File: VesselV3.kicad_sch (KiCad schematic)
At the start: 376 parts, among them J1 JTAG/SWD 10pins Headers, Y1 25MHz

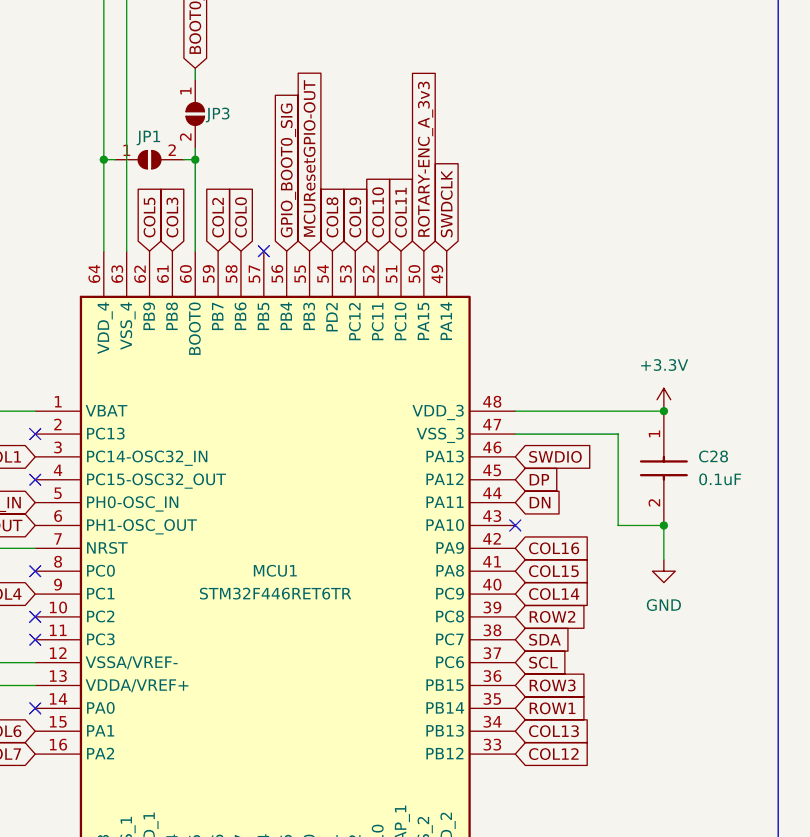
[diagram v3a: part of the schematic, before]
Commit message: FMPI²c to I²c Swap and routing fix
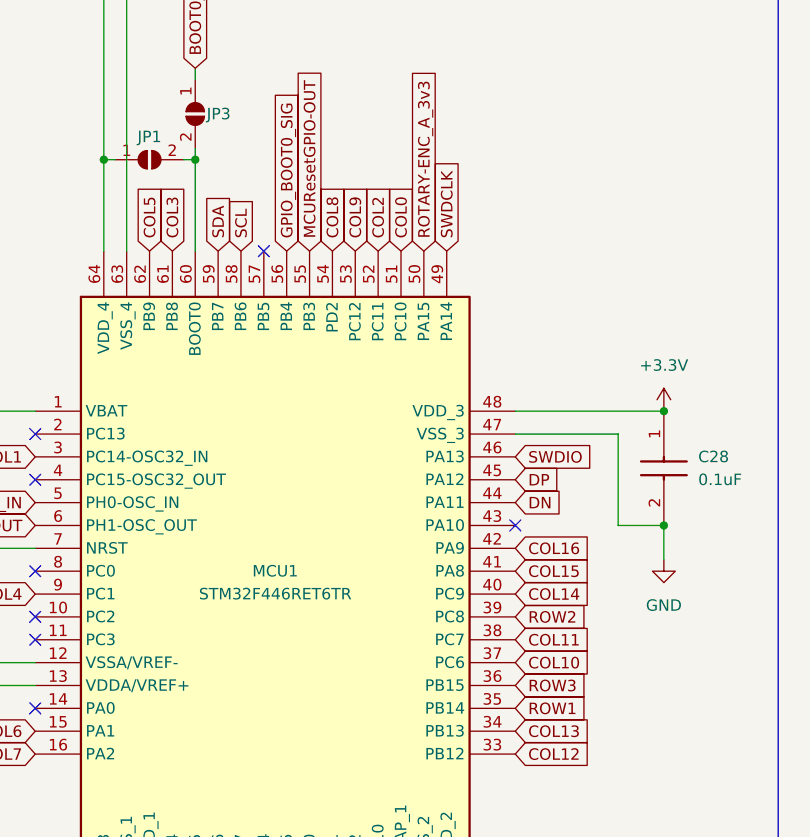
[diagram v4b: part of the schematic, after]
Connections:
- net COL0: now also MCU1.51 (PC10); no longer MCU1.58 (PB6)
- net COL10: now also MCU1.37 (PC6); no longer MCU1.52 (PC11)
- net COL11: now also MCU1.38 (PC7); no longer MCU1.51 (PC10)
- net COL2: now also MCU1.52 (PC11); no longer MCU1.59 (PB7)
- net SCL: now also MCU1.58 (PB6); no longer MCU1.37 (PC6)
- net SDA: now also MCU1.59 (PB7); no longer MCU1.38 (PC7)
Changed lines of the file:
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@@
     )
   )
-  (global_label "SDA" (shape input) (at 674.37 100.33 0) (fields_autoplaced)
-    (effects (font (size 1.27 1.27)) (justify left))
-    (property "Intersheetrefs" "${INTERSHEET_REFS}" (at 680.9233 100.33 0)
+  (global_label "SDA" (shape input) (at 641.35 57.15 90) (fields_autoplaced)
+    (effects (font (size 1.27 1.27)) (justify left))
+    (property "Intersheetrefs" "${INTERSHEET_REFS}" (at 641.35 50.5967 90)
       (effects (font (size 1.27 1.27)) (justify left) hide)
     )
@@
     )
   )
-  (global_label "COL11" (shape input) (at 661.67 57.15 90) (fields_autoplaced)
-    (effects (font (size 1.27 1.27)) (justify left))
-    (property "Intersheetrefs" "${INTERSHEET_REFS}" (at 661.67 48.1172 90)
+  (global_label "COL11" (shape input) (at 674.37 100.33 0) (fields_autoplaced)
+    (effects (font (size 1.27 1.27)) (justify left))
+    (property "Intersheetrefs" "${INTERSHEET_REFS}" (at 683.4028 100.33 0)
       (effects (font (size 1.27 1.27)) (justify left) hide)
     )
@@
     )
   )
-  (global_label "COL2" (shape input) (at 641.35 57.15 90) (fields_autoplaced)
-    (effects (font (size 1.27 1.27)) (justify left))
-    (property "Intersheetrefs" "${INTERSHEET_REFS}" (at 641.35 49.3267 90)
+  (global_label "COL2" (shape input) (at 659.13 57.15 90) (fields_autoplaced)
+    (effects (font (size 1.27 1.27)) (justify left))
+    (property "Intersheetrefs" "${INTERSHEET_REFS}" (at 659.13 49.3267 90)
       (effects (font (size 1.27 1.27)) (justify left) hide)
     )
@@
     )
   )
-  (global_label "COL0" (shape input) (at 643.89 57.15 90) (fields_autoplaced)
-    (effects (font (size 1.27 1.27)) (justify left))
-    (property "Intersheetrefs" "${INTERSHEET_REFS}" (at 643.89 49.3267 90)
+  (global_label "COL0" (shape input) (at 661.67 57.15 90) (fields_autoplaced)
+    (effects (font (size 1.27 1.27)) (justify left))
+    (property "Intersheetrefs" "${INTERSHEET_REFS}" (at 661.67 49.3267 90)
       (effects (font (size 1.27 1.27)) (justify left) hide)
     )
@@
     )
   )
-  (global_label "COL10" (shape input) (at 659.13 57.15 90) (fields_autoplaced)
-    (effects (font (size 1.27 1.27)) (justify left))
-    (property "Intersheetrefs" "${INTERSHEET_REFS}" (at 659.13 48.1172 90)
+  (global_label "COL10" (shape input) (at 674.37 102.87 0) (fields_autoplaced)
+    (effects (font (size 1.27 1.27)) (justify left))
+    (property "Intersheetrefs" "${INTERSHEET_REFS}" (at 683.4028 102.87 0)
       (effects (font (size 1.27 1.27)) (justify left) hide)
     )
@@
     )
   )
-  (global_label "SCL" (shape input) (at 674.37 102.87 0) (fields_autoplaced)
-    (effects (font (size 1.27 1.27)) (justify left))
-    (property "Intersheetrefs" "${INTERSHEET_REFS}" (at 680.8628 102.87 0)
-      (effects (font (size 1.27 1.27)) (justify left) hide)
-    )
+  (global_label "SCL" (shape input) (at 643.89 57.15 90) (fields_autoplaced)
+    (effects (font (size 1.27 1.27)) (justify left))
+    (property "Intersheetrefs" "${INTERSHEET_REFS}" (at 643.89 50.6572 90)
+      (effects (font (size 1.27 1.27)) (justify left) hide)
+    )

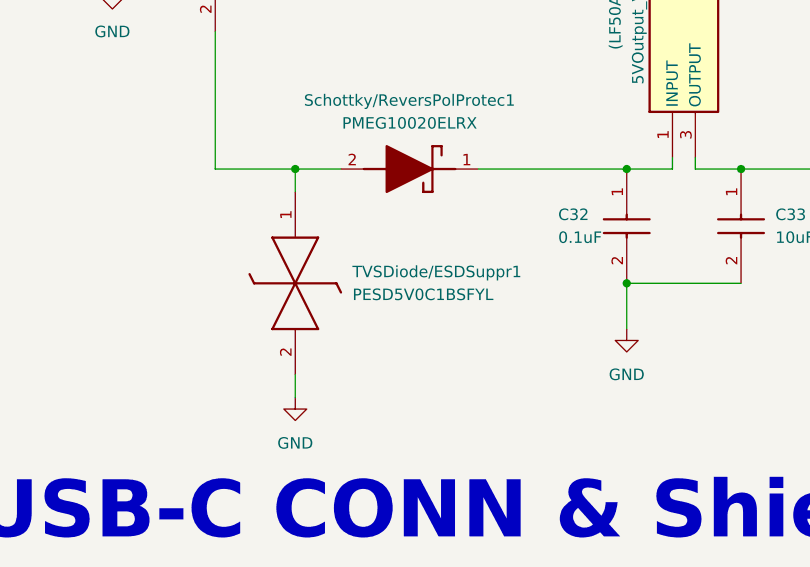
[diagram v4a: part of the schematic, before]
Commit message: Swapped 0402 TVS for SOD123 - Other Routing Fixes
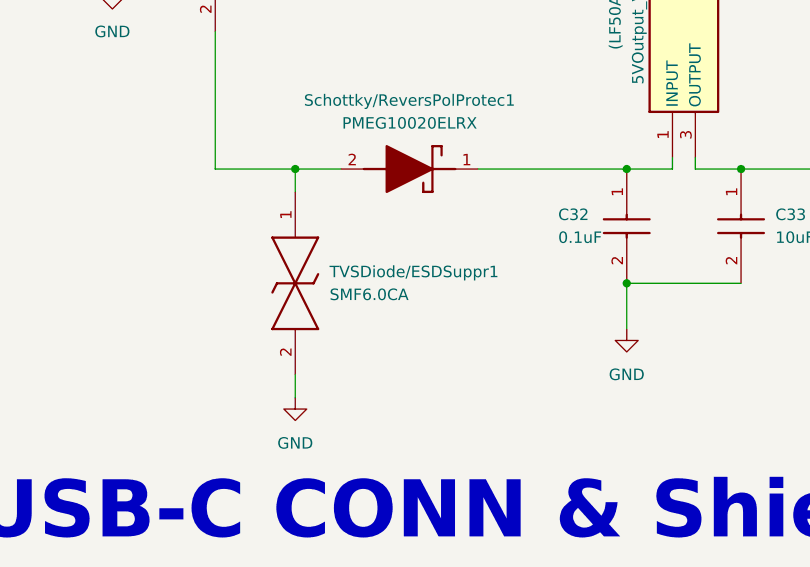
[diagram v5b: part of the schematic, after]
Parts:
- removed TVSDiode/ESDSuppr1: PESD5V0C1BSFYL, SamacSys_Parts:PMEG3005AESFYL, symbol SamacSys_Parts:PESD5V0C1BSFYL
- added TVSDiode/ESDSuppr1: SMF6.0CA, SamacSys_Parts:SODFL3618X108N, symbol SamacSys_Parts:SMF6.0CA
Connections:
- net GND: now also TVSDiode/ESDSuppr1.2
- net at Polyfuse1.2, Schottky/ReversPolProtec1.2 (A): now also TVSDiode/ESDSuppr1.1
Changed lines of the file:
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@@
     )
   )
-  (symbol (lib_id "SamacSys_Parts:PESD5V0C1BSFYL") (at 283.21 86.36 270) (unit 1)
-    (in_bom yes) (on_board yes) (dnp no)
-    (property "Reference" "TVSDiode/ESDSuppr1" (at 289.56 95.25 90)
-      (effects (font (size 1.27 1.27)) (justify left))
-    )
-    (property "Value" "PESD5V0C1BSFYL" (at 289.56 97.79 90)
-      (effects (font (size 1.27 1.27)) (justify left))
-    )
-    (property "Footprint" "SamacSys_Parts:PMEG3005AESFYL" (at 189.56 101.6 0)
-      (effects (font (size 1.27 1.27)) (justify left bottom) hide)
-    )
-    (property "Datasheet" "https://assets.nexperia.com/documents/data-sheet/PESD5V0C1BSF.pdf" (at 89.56 101.6 0)
-      (effects (font (size 1.27 1.27)) (justify left bottom) hide)
-    )
-    (property "Height" "" (at -110.44 101.6 0)
-      (effects (font (size 1.27 1.27)) (justify left bottom) hide)
-    )
-    (property "Mouser Part Number" "771-PESD5V0C1BSFYL" (at -210.44 101.6 0)
-      (effects (font (size 1.27 1.27)) (justify left bottom) hide)
-    )
-    (property "Mouser Price/Stock" "https://www.mouser.co.uk/ProductDetail/Nexperia/PESD5V0C1BSFYL?qs=Pve5fMu%2FDEv%252BAQF4BlT7Aw%3D%3D" (at -310.44 101.6 0)
-      (effects (font (size 1.27 1.27)) (justify left bottom) hide)
-    )
-    (property "Manufacturer_Name" "Nexperia" (at -410.44 101.6 0)
-      (effects (font (size 1.27 1.27)) (justify left bottom) hide)
-    )
-    (property "Manufacturer_Part_Number" "PESD5V0C1BSFYL" (at -510.44 101.6 0)
-      (effects (font (size 1.27 1.27)) (justify left bottom) hide)
-    )
-    (property "DigikeyPartNumber" "ESD9B5.0ST5GOSTR-ND" (at 283.21 86.36 0)
-      (effects (font (size 1.27 1.27)) hide)
-    )
-    (pin "1")
-    (pin "2")
-    (instances
-      (project "VesselV3"
-        (path "/7364f6a3-b999-47c8-8f6d-f83e5421d1ed"
-          (reference "TVSDiode/ESDSuppr1") (unit 1)
-        )
-      )
-    )
-  )
   (symbol (lib_id "SamacSys_Parts:0402ZC103JAT2A") (at 633.73 260.35 270) (unit 1)
     (in_bom yes) (on_board yes) (dnp no) (fields_autoplaced)
@@
         )
       )
+    )
+  )
+  (symbol (lib_id "SamacSys_Parts:SMF6.0CA") (at 283.21 86.36 270) (unit 1)
+    (in_bom yes) (on_board yes) (dnp no) (fields_autoplaced)
+    (property "Reference" "TVSDiode/ESDSuppr1" (at 287.02 95.25 90)
+      (effects (font (size 1.27 1.27)) (justify left))
+    )
+    (property "Value" "SMF6.0CA" (at 287.02 97.79 90)
+      (effects (font (size 1.27 1.27)) (justify left))
+    )
+    (property "Footprint" "SamacSys_Parts:SODFL3618X108N" (at 189.56 99.06 0)
+      (effects (font (size 1.27 1.27)) (justify left bottom) hide)
+    )
+    (property "Datasheet" "https://componentsearchengine.com/Datasheets/1/SMF6.0CA.pdf" (at 89.56 99.06 0)
+      (effects (font (size 1.27 1.27)) (justify left bottom) hide)
+    )
+    (property "Height" "1.08" (at -110.44 99.06 0)
+      (effects (font (size 1.27 1.27)) (justify left bottom) hide)
+    )
+    (property "Mouser Part Number" "576-SMF6.0CA" (at -210.44 99.06 0)
+      (effects (font (size 1.27 1.27)) (justify left bottom) hide)
+    )
+    (property "Mouser Price/Stock" "https://www.mouser.co.uk/ProductDetail/Littelfuse/SMF6.0CA?qs=d0WKAl%252BL4KbbYPeuk1g0Rg%3D%3D" (at -310.44 99.06 0)
+      (effects (font (size 1.27 1.27)) (justify left bottom) hide)
+    )
+    (property "Manufacturer_Name" "LITTELFUSE" (at -410.44 99.06 0)
+      (effects (font (size 1.27 1.27)) (justify left bottom) hide)
+    )
+    (property "Manufacturer_Part_Number" "SMF6.0CA" (at -510.44 99.06 0)
+      (effects (font (size 1.27 1.27)) (justify left bottom) hide)
+    )
+    (property "DigikeyPartNumber" "18-SMF6.0CATR-ND" (at 283.21 86.36 0)
+      (effects (font (size 1.27 1.27)) hide)
+    )
+    (pin "1")
+    (pin "2")
+    (instances
+      (project "VesselV3"
+        (path "/7364f6a3-b999-47c8-8f6d-f83e5421d1ed"
+          (reference "TVSDiode/ESDSuppr1") (unit 1)
+        )
+      )

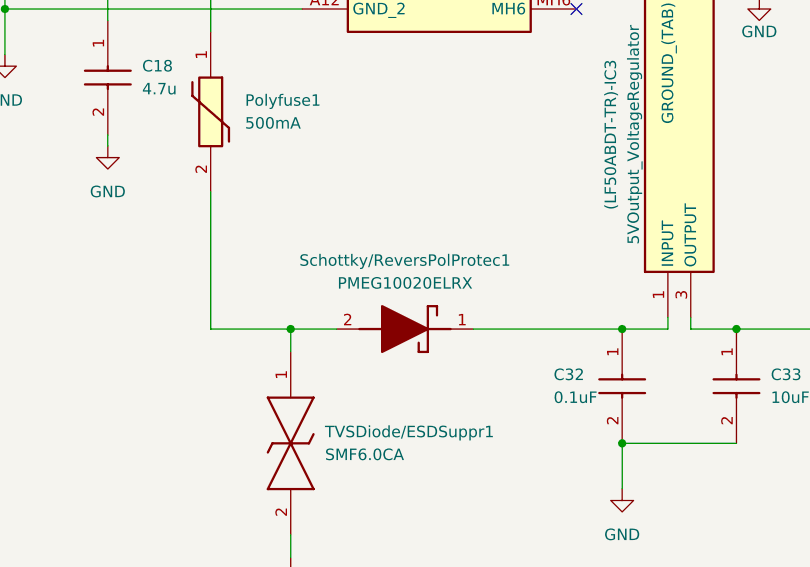
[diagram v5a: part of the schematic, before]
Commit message: Swapped Schottky Rectifier for lower Vf
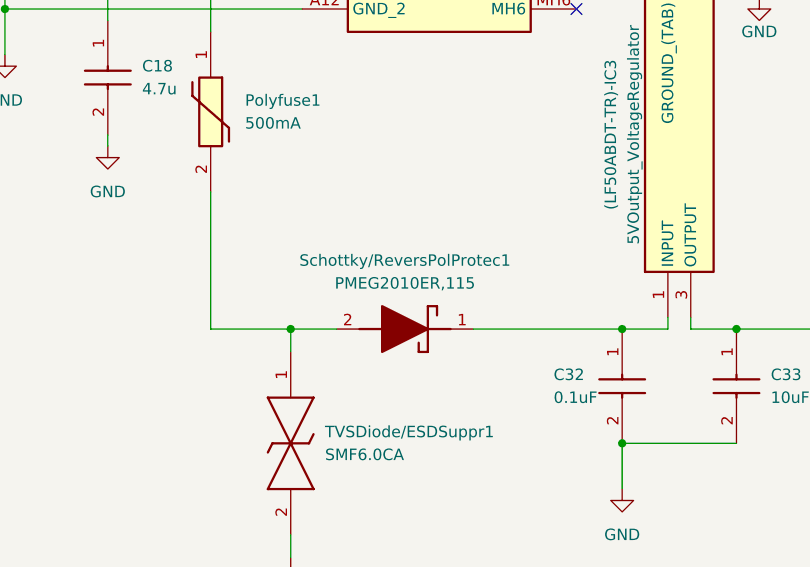
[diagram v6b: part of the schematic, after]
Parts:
- removed Schottky/ReversPolProtec1: PMEG10020ELRX, SamacSys_Parts:SODFL3517X110N, symbol SamacSys_Parts:PMEG10020ELRX
- added Schottky/ReversPolProtec1: PMEG2010ER,115, SamacSys_Parts:PMEG2010ER115, symbol SamacSys_Parts:PMEG2010ER,115
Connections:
- net at (LF50ABDT-TR)-IC3.1 (INPUT), C32.1: now also Schottky/ReversPolProtec1.1 (K)
- net at Polyfuse1.2, TVSDiode/ESDSuppr1.1: now also Schottky/ReversPolProtec1.2 (A)
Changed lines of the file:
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@@
     )
   )
-  (symbol (lib_id "SamacSys_Parts:PMEG10020ELRX") (at 306.07 83.82 180) (unit 1)
-    (in_bom yes) (on_board yes) (dnp no) (fields_autoplaced)
-    (property "Reference" "Schottky/ReversPolProtec1" (at 295.91 76.2 0)
-      (effects (font (size 1.27 1.27)))
-    )
-    (property "Value" "PMEG10020ELRX" (at 295.91 78.74 0)
-      (effects (font (size 1.27 1.27)))
-    )
-    (property "Footprint" "SamacSys_Parts:SODFL3517X110N" (at 293.37 -9.83 0)
-      (effects (font (size 1.27 1.27)) (justify left top) hide)
-    )
-    (property "Datasheet" "https://assets.nexperia.com/documents/data-sheet/PMEG10020ELR.pdf" (at 293.37 -109.83 0)
-      (effects (font (size 1.27 1.27)) (justify left top) hide)
-    )
-    (property "Height" "1.1" (at 293.37 -309.83 0)
-      (effects (font (size 1.27 1.27)) (justify left top) hide)
-    )
-    (property "Mouser Part Number" "771-PMEG10020ELRX" (at 293.37 -409.83 0)
-      (effects (font (size 1.27 1.27)) (justify left top) hide)
-    )
-    (property "Mouser Price/Stock" "https://www.mouser.co.uk/ProductDetail/Nexperia/PMEG10020ELRX?qs=bel5lzaZNxQmrosujSY5VA%3D%3D" (at 293.37 -509.83 0)
-      (effects (font (size 1.27 1.27)) (justify left top) hide)
-    )
-    (property "Manufacturer_Name" "Nexperia" (at 293.37 -609.83 0)
-      (effects (font (size 1.27 1.27)) (justify left top) hide)
-    )
-    (property "Manufacturer_Part_Number" "PMEG10020ELRX" (at 293.37 -709.83 0)
-      (effects (font (size 1.27 1.27)) (justify left top) hide)
-    )
-    (property "DigikeyPartNumber" "1727-2396-2-ND" (at 306.07 83.82 0)
-      (effects (font (size 1.27 1.27)) hide)
-    )
-    (pin "1")
-    (pin "2")
-    (instances
-      (project "VesselV3"
-        (path "/7364f6a3-b999-47c8-8f6d-f83e5421d1ed"
-          (reference "Schottky/ReversPolProtec1") (unit 1)
-        )
-      )
-    )
-  )
   (symbol (lib_id "WS2812BNano4684RGB-3rdParty:4684") (at 454.66 421.64 0) (mirror y) (unit 1)
     (in_bom yes) (on_board yes) (dnp no)
@@
         )
       )
+    )
+  )
+  (symbol (lib_id "SamacSys_Parts:PMEG2010ER,115") (at 306.07 83.82 180) (unit 1)
+    (in_bom yes) (on_board yes) (dnp no) (fields_autoplaced)
+    (property "Reference" "Schottky/ReversPolProtec1" (at 295.91 76.2 0)
+      (effects (font (size 1.27 1.27)))
+    )
+    (property "Value" "PMEG2010ER,115" (at 295.91 78.74 0)
+      (effects (font (size 1.27 1.27)))
+    )
+    (property "Footprint" "SamacSys_Parts:PMEG2010ER115" (at 293.37 -9.83 0)
+      (effects (font (size 1.27 1.27)) (justify left top) hide)
+    )
+    (property "Datasheet" "https://assets.nexperia.com/documents/data-sheet/PMEG2010ER.pdf" (at 293.37 -109.83 0)
+      (effects (font (size 1.27 1.27)) (justify left top) hide)
+    )
+    (property "Height" "1.1" (at 293.37 -309.83 0)
+      (effects (font (size 1.27 1.27)) (justify left top) hide)
+    )
+    (property "Mouser Part Number" "771-PMEG2010ER115" (at 293.37 -409.83 0)
+      (effects (font (size 1.27 1.27)) (justify left top) hide)
+    )
+    (property "Mouser Price/Stock" "https://www.mouser.co.uk/ProductDetail/Nexperia/PMEG2010ER115?qs=LMSg3oBIm%2FjLN28PGE8ULg%3D%3D" (at 293.37 -509.83 0)
+      (effects (font (size 1.27 1.27)) (justify left top) hide)
+    )
+    (property "Manufacturer_Name" "Nexperia" (at 293.37 -609.83 0)
+      (effects (font (size 1.27 1.27)) (justify left top) hide)
+    )
+    (property "Manufacturer_Part_Number" "PMEG2010ER,115" (at 293.37 -709.83 0)
+      (effects (font (size 1.27 1.27)) (justify left top) hide)
+    )
+    (property "DigikeyPartNumber" "1727-5192-2-ND" (at 306.07 83.82 0)
+      (effects (font (size 1.27 1.27)) hide)
+    )
+    (pin "1")
+    (pin "2")
+    (instances
+      (project "VesselV3"
+        (path "/7364f6a3-b999-47c8-8f6d-f83e5421d1ed"
+          (reference "Schottky/ReversPolProtec1") (unit 1)
+        )
+      )

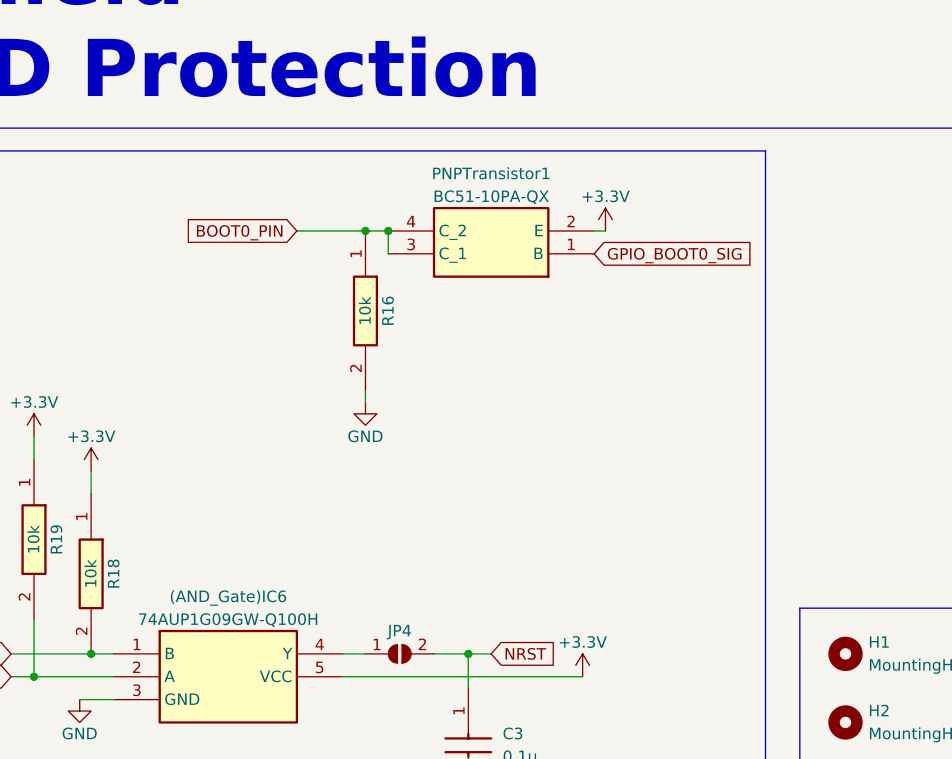
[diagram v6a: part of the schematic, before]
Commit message: Swapped PNP Transistor QFN for SOT123 Package- Updated PMMA
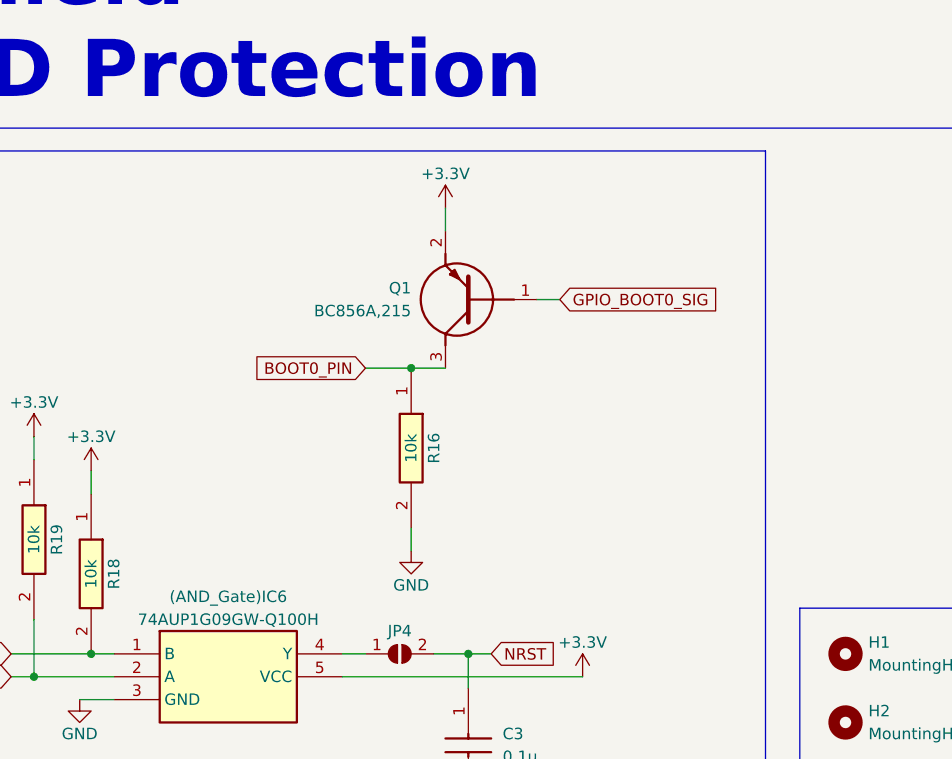
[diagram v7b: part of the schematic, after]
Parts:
- removed PNPTransistor1: BC51-10PA-QX, SamacSys_Parts:BC55PASQX, symbol SamacSys_Parts:BC51-10PA-QX
- added Q1: BC856A,215, SamacSys_Parts:SOT95P230X110-3N, symbol SamacSys_Parts:BC856A,215
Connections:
- net +3.3V: now also Q1.2 (E)
- net BOOT0_PIN: now also Q1.3 (C)
- net GPIO_BOOT0_SIG: now also Q1.1 (B)
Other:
- moved on the sheet: R16
